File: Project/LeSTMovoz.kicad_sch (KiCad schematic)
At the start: 115 parts, among them J1 USB_C_Receptacle_USB2.0, SW1 SKQGABE010, U1 STM32F072RBTx, U2 L78L33_TO92, U3 74AHCT1G125

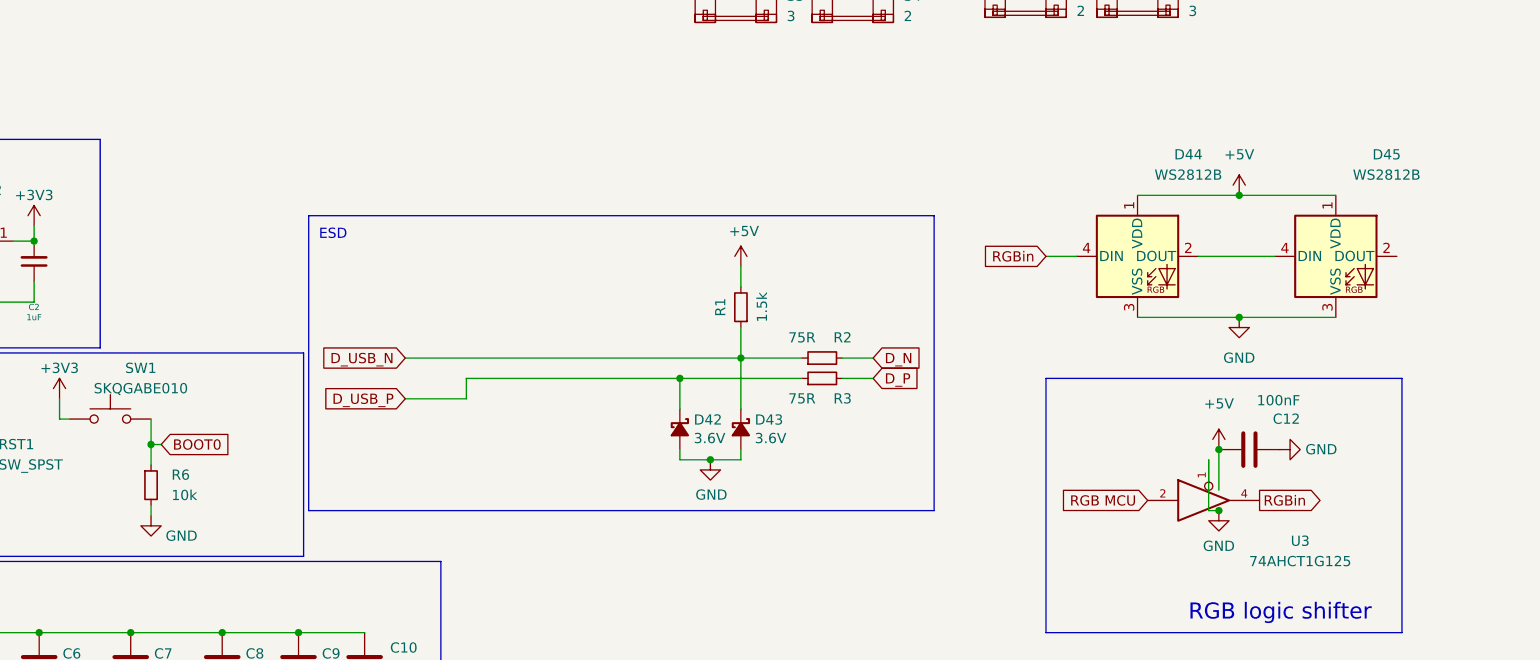
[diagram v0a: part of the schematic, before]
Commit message: changed rgb component, 10k for 2*5k1 resistors, finished THT BOM
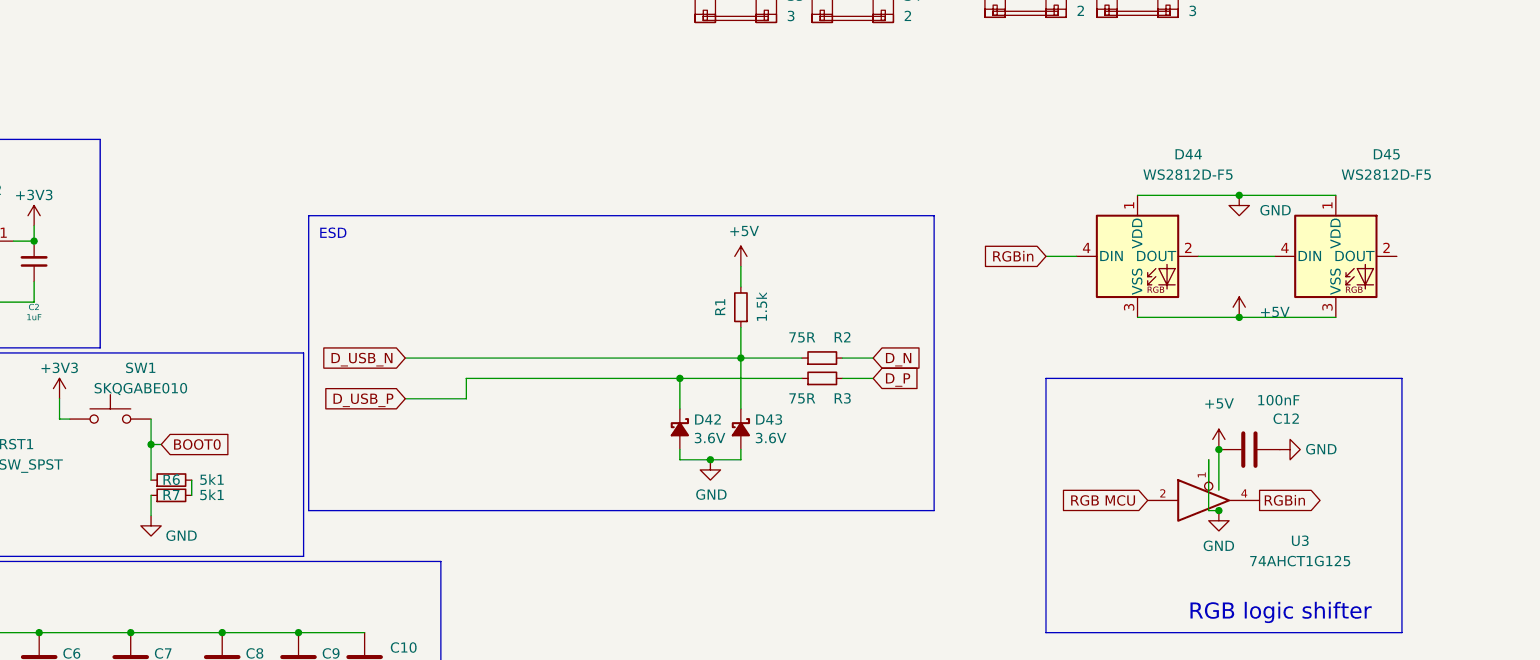
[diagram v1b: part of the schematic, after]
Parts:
- added R7: 5k1, Resistor_THT:R_Axial_DIN0204_L3.6mm_D1.6mm_P7.62mm_Horizontal, symbol Device:R_Small
- D44, D45: value WS2812B -> WS2812D-F5
- R6: value 10k -> 5k1
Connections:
- net +5V: now also D44.3 (VSS), D45.3 (VSS); no longer D44.1 (VDD), D45.1 (VDD)
- net GND: now also D44.1 (VDD), D45.1 (VDD), R7.1; no longer D44.3 (VSS), D45.3 (VSS), R6.2
- new net: R6.2, R7.2
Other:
- moved on the sheet: R6
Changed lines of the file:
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@@
   (junction (at 24.13 186.055) (diameter 0) (color 0 0 0 0)
   )
+  (junction (at 247.65 125.73) (diameter 0) (color 0 0 0 0)
+  )
   (junction (at 44.45 17.78) (diameter 0) (color 0 0 0 0)
   )
@@
   (junction (at 175.895 38.735) (diameter 0) (color 0 0 0 0)
   )
+  (junction (at 247.65 140.97) (diameter 0) (color 0 0 0 0)
+  )
   (junction (at 183.515 26.67) (diameter 0) (color 0 0 0 0)
   )
@@
   (junction (at 145.415 62.23) (diameter 0) (color 0 0 0 0)
   )
-  (junction (at 247.65 125.73) (diameter 0) (color 0 0 0 0)
-  )
   (junction (at 196.215 44.45) (diameter 0) (color 0 0 0 0)
   )
@@
   (junction (at 196.215 80.01) (diameter 0) (color 0 0 0 0)
   )
-  (junction (at 247.65 140.97) (diameter 0) (color 0 0 0 0)
-  )
   (junction (at 245.11 165.1) (diameter 0) (color 0 0 0 0)
   )
@@
     (stroke (width 0) (type default))
   )
-  (wire (pts (xy 247.65 140.97) (xy 259.715 140.97))
-    (stroke (width 0) (type default))
-  )
   (wire (pts (xy 177.8 157.48) (xy 177.8 158.75))
     (stroke (width 0) (type default))
@@
     (stroke (width 0) (type default))
   )
-  (wire (pts (xy 247.65 125.73) (xy 259.715 125.73))
-    (stroke (width 0) (type default))
-  )
   (wire (pts (xy 170.815 44.45) (xy 170.815 62.23))
     (stroke (width 0) (type default))
@@
     (stroke (width 0) (type default))
   )
-  (wire (pts (xy 111.76 156.845) (xy 111.76 159.385))
+  (wire (pts (xy 111.76 156.845) (xy 111.76 161.29))
     (stroke (width 0) (type default))
   )
@@
     (stroke (width 0) (type default))
   )
+  (wire (pts (xy 247.65 125.73) (xy 259.715 125.73))
+    (stroke (width 0) (type default))
+  )
   (wire (pts (xy 150.495 38.1) (xy 150.495 38.735))
     (stroke (width 0) (type default))
@@
     (stroke (width 0) (type default))
   )
+  (wire (pts (xy 116.84 161.29) (xy 116.84 163.195))
+    (stroke (width 0) (type default))
+  )
   (wire (pts (xy 82.55 163.195) (xy 82.55 162.56))
     (stroke (width 0) (type default))
@@
     (stroke (width 0) (type default))
   )
-  (wire (pts (xy 111.76 164.465) (xy 111.76 165.735))
+  (wire (pts (xy 111.76 163.195) (xy 111.76 165.735))
     (stroke (width 0) (type default))
   )
@@
     (stroke (width 0) (type default))
   )
+  (wire (pts (xy 247.65 140.97) (xy 259.715 140.97))
+    (stroke (width 0) (type default))
+  )
   (wire (pts (xy 41.91 17.78) (xy 44.45 17.78))
     (stroke (width 0) (type default))
@@
       (effects (font (size 1.27 1.27)))
     )
-    (property "Value" "WS2812B" (at 241.3 123.19 0)
+    (property "Value" "WS2812D-F5 " (at 241.3 123.19 0)
       (effects (font (size 1.27 1.27)))
     )
@@
       (effects (font (size 1.27 1.27)))
     )
-    (property "Value" "WS2812B" (at 266.065 123.19 0)
+    (property "Value" "WS2812D-F5 " (at 266.065 123.19 0)
       (effects (font (size 1.27 1.27)))
     )
@@
     )
   )
-  (symbol (lib_id "power:GND") (at 247.65 140.97 0) (unit 1)
+  (symbol (lib_id "power:GND") (at 247.65 125.73 0) (unit 1)
     (in_bom yes) (on_board yes) (dnp no) (fields_autoplaced)
-    (property "Reference" "#PWR020" (at 247.65 147.32 0)
+    (property "Reference" "#PWR020" (at 247.65 132.08 0)
       (effects (font (size 1.27 1.27)) hide)
     )
-    (property "Value" "GND" (at 247.65 146.05 0)
-      (effects (font (size 1.27 1.27)))
+    (property "Value" "GND" (at 250.19 127.635 0)
+      (effects (font (size 1.27 1.27)) (justify left))
     )
-    (property "Footprint" "" (at 247.65 140.97 0)
+    (property "Footprint" "" (at 247.65 125.73 0)
       (effects (font (size 1.27 1.27)) hide)
     )
-    (property "Datasheet" "" (at 247.65 140.97 0)
+    (property "Datasheet" "" (at 247.65 125.73 0)
       (effects (font (size 1.27 1.27)) hide)
     )
@@
     )
   )
-  (symbol (lib_id "Device:R_Small") (at 111.76 161.925 0) (unit 1)
-    (in_bom yes) (on_board yes) (dnp no) (fields_autoplaced)
-    (property "Reference" "R6" (at 114.3 160.6549 0)
-      (effects (font (size 1.27 1.27)) (justify left))
+  (symbol (lib_id "Device:R_Small") (at 114.3 161.29 90) (unit 1)
+    (in_bom yes) (on_board yes) (dnp no)
+    (property "Reference" "R6" (at 114.3 161.29 90)
+      (effects (font (size 1.27 1.27)))
     )
-    (property "Value" "10k" (at 114.3 163.1949 0)
-      (effects (font (size 1.27 1.27)) (justify left))
+    (property "Value" "5k1" (at 119.38 161.29 90)
+      (effects (font (size 1.27 1.27)))
     )
-    (property "Footprint" "Resistor_THT:R_Axial_DIN0204_L3.6mm_D1.6mm_P7.62mm_Horizontal" (at 111.76 161.925 0)
+    (property "Footprint" "Resistor_THT:R_Axial_DIN0204_L3.6mm_D1.6mm_P7.62mm_Horizontal" (at 114.3 161.29 0)
       (effects (font (size 1.27 1.27)) hide)
     )
-    (property "Datasheet" "~" (at 111.76 161.925 0)
+    (property "Datasheet" "~" (at 114.3 161.29 0)
       (effects (font (size 1.27 1.27)) hide)
     )
@@
     )
   )
+  (symbol (lib_id "Device:R_Small") (at 114.3 163.195 90) (unit 1)
+    (in_bom yes) (on_board yes) (dnp no)
+    (property "Reference" "R7" (at 114.3 163.195 90)
+      (effects (font (size 1.27 1.27)))
+    )
+    (property "Value" "5k1" (at 119.38 163.195 90)
+      (effects (font (size 1.27 1.27)))
+    )
+    (property "Footprint" "Resistor_THT:R_Axial_DIN0204_L3.6mm_D1.6mm_P7.62mm_Horizontal" (at 114.3 163.195 0)
+      (effects (font (size 1.27 1.27)) hide)
+    )
+    (property "Datasheet" "~" (at 114.3 163.195 0)
+      (effects (font (size 1.27 1.27)) hide)
+    )
+    (pin "1")
+    (pin "2")
+    (instances
+      (project "LeSTMovoz"
+        (path "/224b9503-d71c-4dda-b22e-ce41540eaab0"
+          (reference "R7") (unit 1)
+        )
+      )
+      (project "RP2040-Guide"
+        (path "/ba62e47e-9e07-4e97-ab08-24b670d50f97"
+          (reference "R3") (unit 1)
+        )
+      )
+      (project "PLACER TEST"
+        (path "/de2aa960-84be-4499-a5ee-bb1f2ca3c0f1"
+          (reference "R2") (unit 1)
+        )
+      )
+      (project "forti"
+        (path "/f5e5948c-eeca-4160-a5f8-686f765d01ce"
+          (reference "R1") (unit 1)
+        )
+      )
+    )
+  )
   (symbol (lib_id "Device:D_Small") (at 276.86 71.12 90) (unit 1)
     (in_bom yes) (on_board yes) (dnp no)
@@
     )
   )
-  (symbol (lib_id "power:+5V") (at 247.65 125.73 0) (unit 1)
+  (symbol (lib_id "power:+5V") (at 247.65 140.97 0) (unit 1)
     (in_bom yes) (on_board yes) (dnp no) (fields_autoplaced)
-    (property "Reference" "#PWR019" (at 247.65 129.54 0)
+    (property "Reference" "#PWR019" (at 247.65 144.78 0)
       (effects (font (size 1.27 1.27)) hide)
     )
-    (property "Value" "+5V" (at 247.65 120.65 0)
-      (effects (font (size 1.27 1.27)))
+    (property "Value" "+5V" (at 250.19 140.335 0)
+      (effects (font (size 1.27 1.27)) (justify left))
     )
-    (property "Footprint" "" (at 247.65 125.73 0)
+    (property "Footprint" "" (at 247.65 140.97 0)
       (effects (font (size 1.27 1.27)) hide)
     )
-    (property "Datasheet" "" (at 247.65 125.73 0)
+    (property "Datasheet" "" (at 247.65 140.97 0)
       (effects (font (size 1.27 1.27)) hide)
     )

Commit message: revison work
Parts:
- D44, D45: value WS2812D-F5 -> WS2812D-F5
